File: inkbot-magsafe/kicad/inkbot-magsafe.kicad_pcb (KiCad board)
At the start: 4 copper layers, 60 x 99 mm, 69 parts, among them J1 Hirose_FH12-24S-0.5SH_1x24-1M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, J2 Molex_Pico-EZmate_78171-0003_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, J3 Coil_SolderPads, Q1 SOT-323_SC-70, U1 Raytac_MDBT50Q, U2 Texas_VQFN-RHL-20, U3 BQ25185_DLH0010A, U4 SOT-23-5, Y1 Crystal_SMD_3215-2Pin_3.2x1.5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

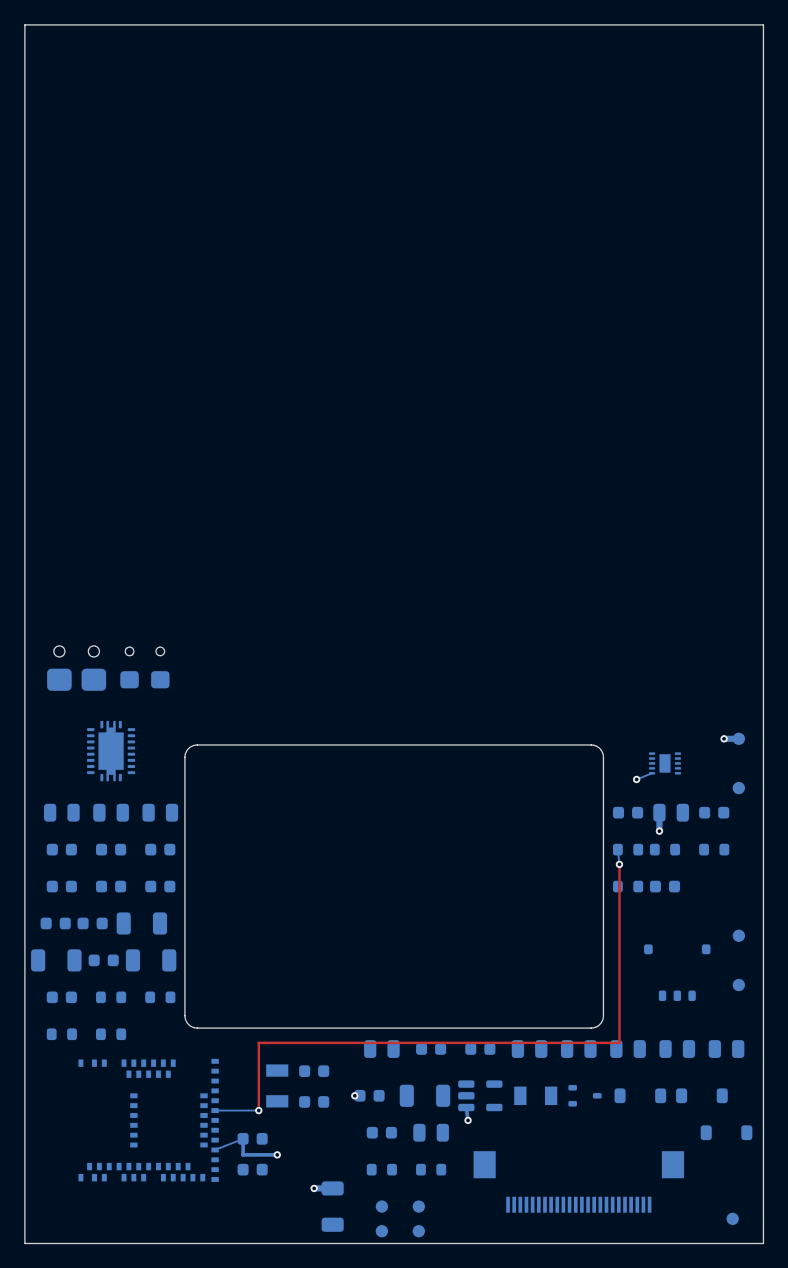
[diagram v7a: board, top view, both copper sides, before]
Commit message: inkbot-magsafe: commit clean routed board
Co-authored-by: Jason Hall <imjasonh@users.noreply.github.com>
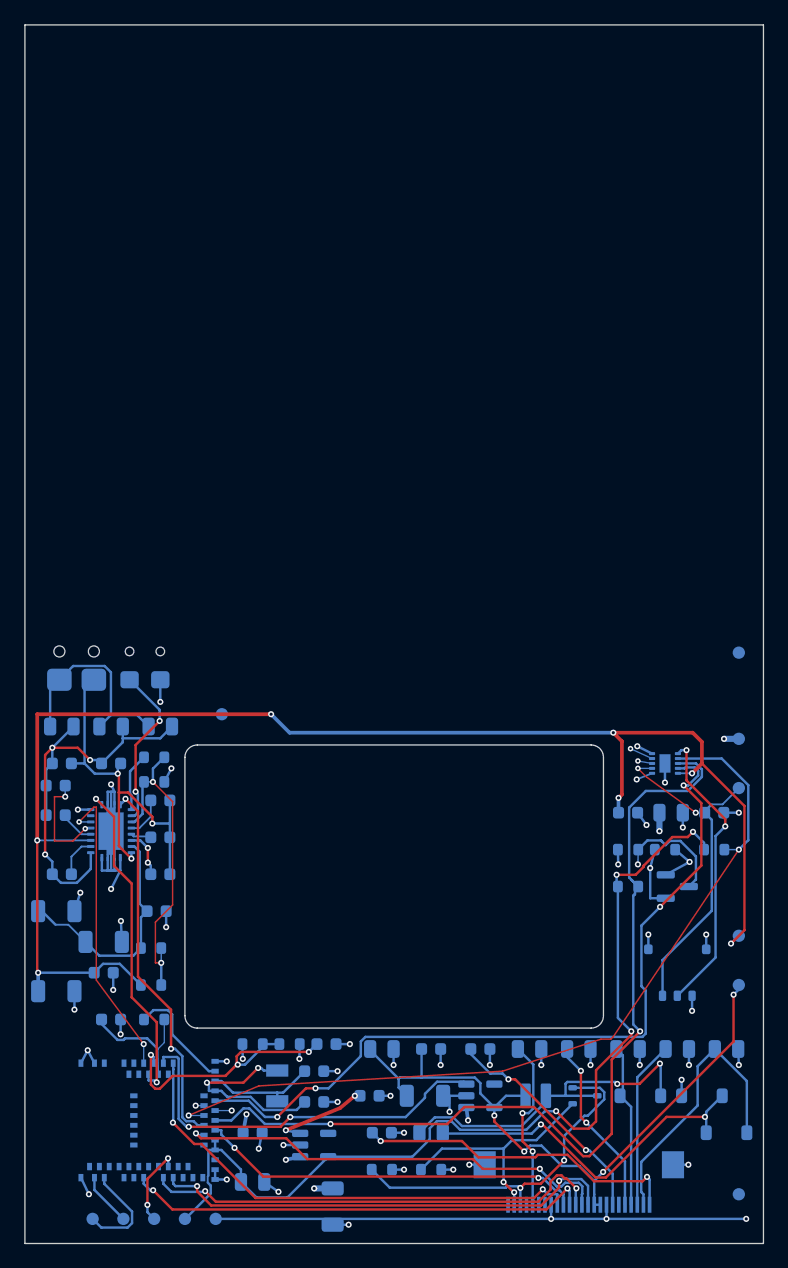
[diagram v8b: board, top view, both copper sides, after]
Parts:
- added FID1: Fiducial_1mm_Mask2mm, Fiducial:Fiducial_1mm_Mask2mm, B.Cu at (16.0, 56.0)
- added FID2: Fiducial_1mm_Mask2mm, Fiducial:Fiducial_1mm_Mask2mm, B.Cu at (58.0, 51.0)
- added FID3: Fiducial_1mm_Mask2mm, Fiducial:Fiducial_1mm_Mask2mm, B.Cu at (58.0, 95.0)
- added Q2: SOT-23, Package_TO_SOT_SMD:SOT-23, B.Cu at (53.0, 70.0)
- added R10: R_0603_1608Metric, Resistor_SMD:R_0603_1608Metric, B.Cu at (21.5, 82.8)
- added R13: R_0603_1608Metric, Resistor_SMD:R_0603_1608Metric, B.Cu at (10.5, 80.8)
- added R9: R_0603_1608Metric, Resistor_SMD:R_0603_1608Metric, B.Cu at (18.5, 82.8)
- added RT3: C_0603_1608Metric, Capacitor_SMD:C_0603_1608Metric, B.Cu at (7.00, 80.8)
- added U5: SOT-23-5, Package_TO_SOT_SMD:SOT-23-5, B.Cu at (23.5, 91.0)
- C22: value C_0603_1608Metric -> C_0805_2012Metric; footprint Capacitor_SMD:C_0603_1608Metric -> Capacitor_SMD:C_0805_2012Metric
- L1: value L_TDK_NLV25_2.5x2.0mm -> TDK_VLS252010CX; footprint Inductor_SMD:L_TDK_NLV25_2.5x2.0mm -> inkbot_magsafe:TDK_VLS252010CX
- U3: value BQ25185_DLH0010A -> TI_DLH0010A_WSON-10; footprint inkbot_magsafe:BQ25185_DLH0010A -> inkbot_magsafe:TI_DLH0010A_WSON-10
- moved TP5 42.0 mm to (15.5, 97.0)
- moved C20 30.3 mm to (24.5, 82.8)
- moved TP2 24.0 mm to (8.00, 97.0)
- moved TP1 23.5 mm to (5.50, 97.0)
- moved R1 19.8 mm to (10.5, 59.5)
- moved TP4 19.0 mm to (13.0, 97.0)
- moved TP3 18.5 mm to (10.5, 97.0)
- moved R2 17.5 mm to (10.5, 61.5)
- moved C11 11.4 mm to (11.0, 63.0)
- moved C10 11.2 mm to (2.50, 61.8), turned to 180 degrees
- moved R3 10.1 mm to (10.2, 75.0)
- moved C6 8.25 mm to (3.00, 69.0), turned to 180 degrees
- moved C15 8.10 mm to (2.55, 78.5)
- moved C7 8.06 mm to (11.0, 69.0)
- moved C8 7.34 mm to (2.50, 64.2), turned to 180 degrees
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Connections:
- net /CHG_STAT1 renamed /CHG_INT_N
- net /CHG_STAT2 renamed /CHG_PG_N
- C20 pad 1: /CHG_ISET_COMP -> /SYS_SENSE
- C22 pad 1: /VDD_NRF -> /MCU_3V0
- R5 pad 1: /CHG_EN_N -> /SYS
- R5 pad 2: GND -> /CHG_CE_N
- R6 pad 1: /CHG_VSET -> /CHG_ENABLE
- R7 pad 1: /CHG_ISET -> /MCU_3V0
- R7 pad 2: GND -> /CHG_SDA
- R8 pad 1: /CHG_ISET -> /MCU_3V0
- R8 pad 2: /CHG_ISET_COMP -> /CHG_SCL
- TP4 pad 1: /VDD_NRF -> /MCU_3V0
- U1 pad 10: (no net) -> /SYS_SENSE
- U1 pad 11: /QI_PRESENT -> /PANEL_TEMP_SENSE
- U1 pad 16: (no net) -> /PANEL_TEMP_EXCITE
- U1 pad 22: /CHG_EN_N -> /CHG_ENABLE
- U1 pad 23: (no net) -> /CHG_SDA
- U1 pad 24: (no net) -> /CHG_SCL
- U1 pad 25: (no net) -> /QI_EN2
- U1 pad 28: /VDD_NRF -> /MCU_3V0
- U1 pad 30: /SYS -> /MCU_3V0
- U1 pad 32: (no net) -> GND
- U1 pad 8: (no net) -> /QI_PRESENT
- U1 pad 9: (no net) -> /QI_EN1
- U2 pad 10: GND -> /QI_EN1
- U2 pad 11: GND -> /QI_EN2
- U3 pad 4: /CHG_EN_N -> /CHG_CE_N
- U3 pad 7: /CHG_VSET -> /CHG_SDA
- U3 pad 8: /CHG_ISET -> /CHG_SCL
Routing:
- net GND: track 0.00 -> 127.6 mm, vias 0 -> 51
- net /QI_OUT: track 0.00 -> 119.5 mm, vias 0 -> 7
- net /MCU_3V0: track 0.00 -> 77.1 mm, vias 0 -> 4
- net /CHG_SCL: track 0.00 -> 74.5 mm, vias 0 -> 2
- net /CHG_SDA: track 0.00 -> 68.4 mm, vias 0 -> 2
- net /CHG_INT_N: track 0.00 -> 65.6 mm, vias 0 -> 4
- net /CHG_PG_N: track 0.00 -> 59.9 mm, vias 0 -> 2
- net /CHG_ENABLE: track 0.00 -> 55.7 mm, vias 0 -> 2
- net /PANEL_3V0: track 0.00 -> 54.5 mm, vias 0 -> 4
- net /CHG_EN_N: track 54.1 -> 0.00 mm, vias 2 -> 0
- net /PANEL_BUSY: track 0.00 -> 39.9 mm, vias 0 -> 2
- net /PANEL_MOSI: track 0.00 -> 38.1 mm, vias 0 -> 2
- net /PANEL_DC: track 0.00 -> 37.9 mm, vias 0 -> 2
- net /PANEL_CS: track 0.00 -> 37.8 mm, vias 0 -> 2
- net /QI_AC1: track 0.00 -> 36.7 mm, vias 0 -> 3
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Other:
- board text added: "GDEY0397T81P panel outline"
- board text added: "LP242030 protected-cell cutout"
- board text removed: "GDEM0397T81P panel outline"
- board text removed: "LP252030 protected-cell cutout"
- board text removed: "orientation magnet"
